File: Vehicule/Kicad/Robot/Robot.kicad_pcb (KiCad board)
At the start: 2 copper layers, 60 x 50 mm, 3 parts, among them U1 ESP32-C3_SUPERMINI, U2 L293D, U3 Regulator-DFR0569

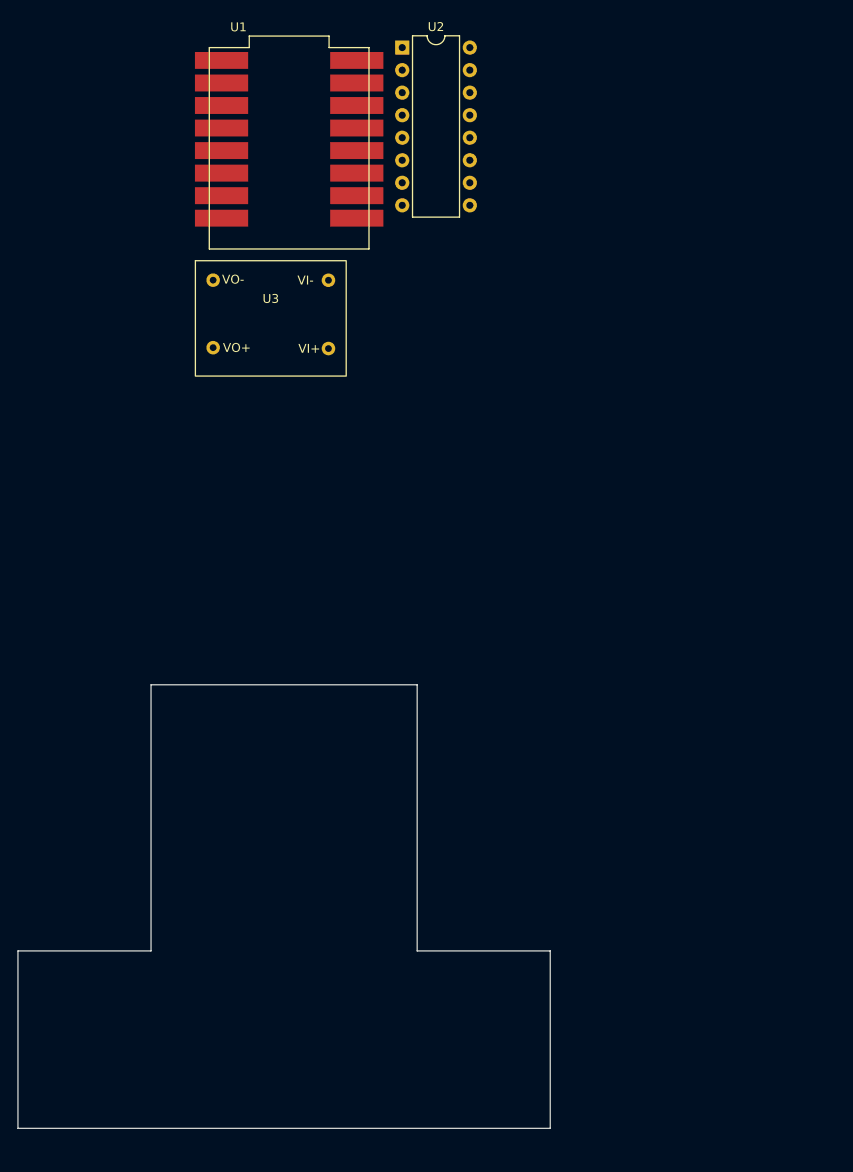
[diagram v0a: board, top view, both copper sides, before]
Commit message: Schema et implantation du circuit pour le robot
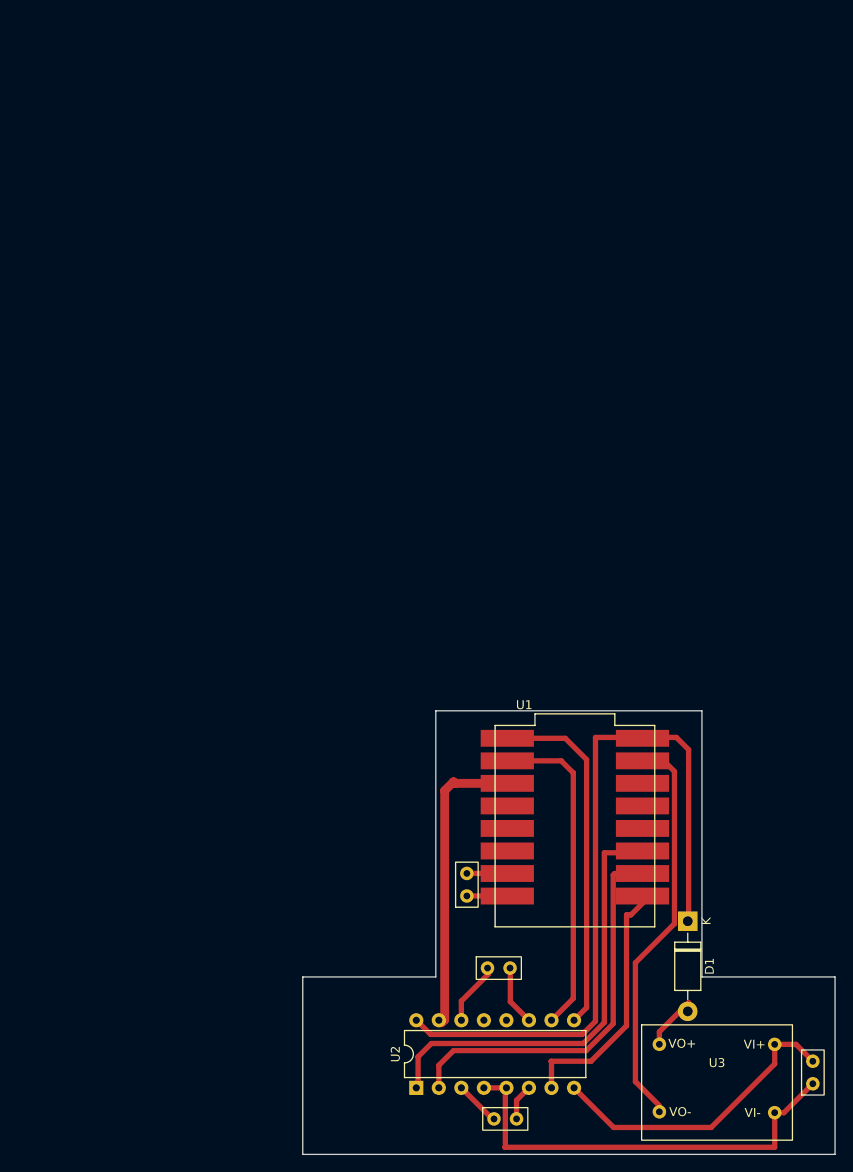
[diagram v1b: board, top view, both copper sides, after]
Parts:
- added D1: 1N5818, Diode_THT:D_DO-41_SOD81_P10.16mm_Horizontal, F.Cu at (115.5, 126.7)
- added J1: Conn_01x02_Socket, Empreintes:CONN-2-PINS, F.Cu at (129.6, 143.7)
- added J2: Conn_01x02_Socket, Empreintes:CONN-2-PINS, F.Cu at (90.6, 122.5)
- added J3: Conn_01x02_Socket, Empreintes:CONN-2-PINS, F.Cu at (94.2, 131.9)
- added J4: Conn_01x02_Socket, Empreintes:CONN-2-PINS, F.Cu at (94.9, 148.9)
- U3: value Regulator-DFR0569 -> ~
- moved U2 117.3 mm to (84.9, 145.4), turned to 90 degrees
- moved U3 99.7 mm to (118.8, 144.3)
- moved U1 82.9 mm to (102.8, 115.9)
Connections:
- U1 pad 0: unconnected-(U1-GPIO0-Pad0) -> Net-(U1-GPIO0)
- U1 pad 1: unconnected-(U1-GPIO1-Pad1) -> Net-(U1-GPIO1)
- U1 pad 2: unconnected-(U1-GPIO2-Pad2) -> Net-(U1-GPIO2)
- U1 pad 20: unconnected-(U1-GPIO20-Pad20) -> Net-(J2-Pin_2)
- U1 pad 21: unconnected-(U1-GPIO21-Pad21) -> Net-(J2-Pin_1)
- U1 pad 3.3: unconnected-(U1-3V3-Pad3.3) -> Net-(U1-3V3)
- U1 pad 5: unconnected-(U1-GPIO5-Pad5) -> Net-(U1-GPIO5)
- U1 pad 5V: unconnected-(U1-Pad5V) -> Net-(D1-K)
- U1 pad 6: unconnected-(U1-GPIO6-Pad6) -> Net-(U1-GPIO6)
- U1 pad 7: unconnected-(U1-GPIO7-Pad7) -> Net-(U1-GPIO7)
- U1 pad G: unconnected-(U1-GND-PadG) -> GND
- U2 pad 1: unconnected-(U2-EN1,2-Pad1) -> Net-(U1-GPIO2)
- U2 pad 10: unconnected-(U2-3A-Pad10) -> Net-(U1-GPIO6)
- U2 pad 11: unconnected-(U2-3Y-Pad11) -> Net-(J3-Pin_2)
- U2 pad 14: unconnected-(U2-4Y-Pad14) -> Net-(J3-Pin_1)
- U2 pad 15: unconnected-(U2-4A-Pad15) -> Net-(U1-GPIO7)
- U2 pad 16: unconnected-(U2-VCC1-Pad16) -> Net-(D1-K)
- U2 pad 2: unconnected-(U2-1A-Pad2) -> Net-(U1-GPIO1)
- U2 pad 3: unconnected-(U2-1Y-Pad3) -> Net-(J4-Pin_1)
- U2 pad 4: unconnected-(U2-GND-Pad4) -> GND
- U2 pad 5: unconnected-(U2-GND-Pad5) -> GND
- U2 pad 6: unconnected-(U2-2Y-Pad6) -> Net-(J4-Pin_2)
- U2 pad 7: unconnected-(U2-2A-Pad7) -> Net-(U1-GPIO0)
- U2 pad 8: unconnected-(U2-VCC2-Pad8) -> Net-(J1-Pin_2)
- U2 pad 9: unconnected-(U2-EN3,4-Pad9) -> Net-(U1-GPIO5)
- U3 pad 1: unconnected-(U3-VO--Pad1) -> Net-(D1-A)
- U3 pad 2: unconnected-(U3-VO+-Pad2) -> GND
- U3 pad 3: unconnected-(U3-VI--Pad3) -> Net-(J1-Pin_2)
- U3 pad 4: unconnected-(U3-VI+-Pad4) -> GND
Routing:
- net GND: track 0.00 -> 94.0 mm
- net Net-(D1-K): track 0.00 -> 81.6 mm
- net Net-(U1-GPIO2): track 0.00 -> 49.7 mm
- net Net-(U1-GPIO1): track 0.00 -> 45.1 mm
- net Net-(U1-GPIO5): track 0.00 -> 39.1 mm
- net Net-(U1-GPIO6): track 0.00 -> 36.1 mm
- net Net-(J1-Pin_2): track 0.00 -> 34.7 mm
- net Net-(U1-GPIO7): track 0.00 -> 33.2 mm
- net Net-(U1-GPIO0): track 0.00 -> 29.2 mm
- net Net-(J3-Pin_1): track 0.00 -> 6.55 mm
- net Net-(J3-Pin_2): track 0.00 -> 6.15 mm
- net Net-(J2-Pin_2): track 0.00 -> 5.38 mm
- net Net-(J2-Pin_1): track 0.00 -> 5.38 mm
- net Net-(D1-A): track 0.00 -> 5.38 mm
- net Net-(J4-Pin_1): track 0.00 -> 5.13 mm
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
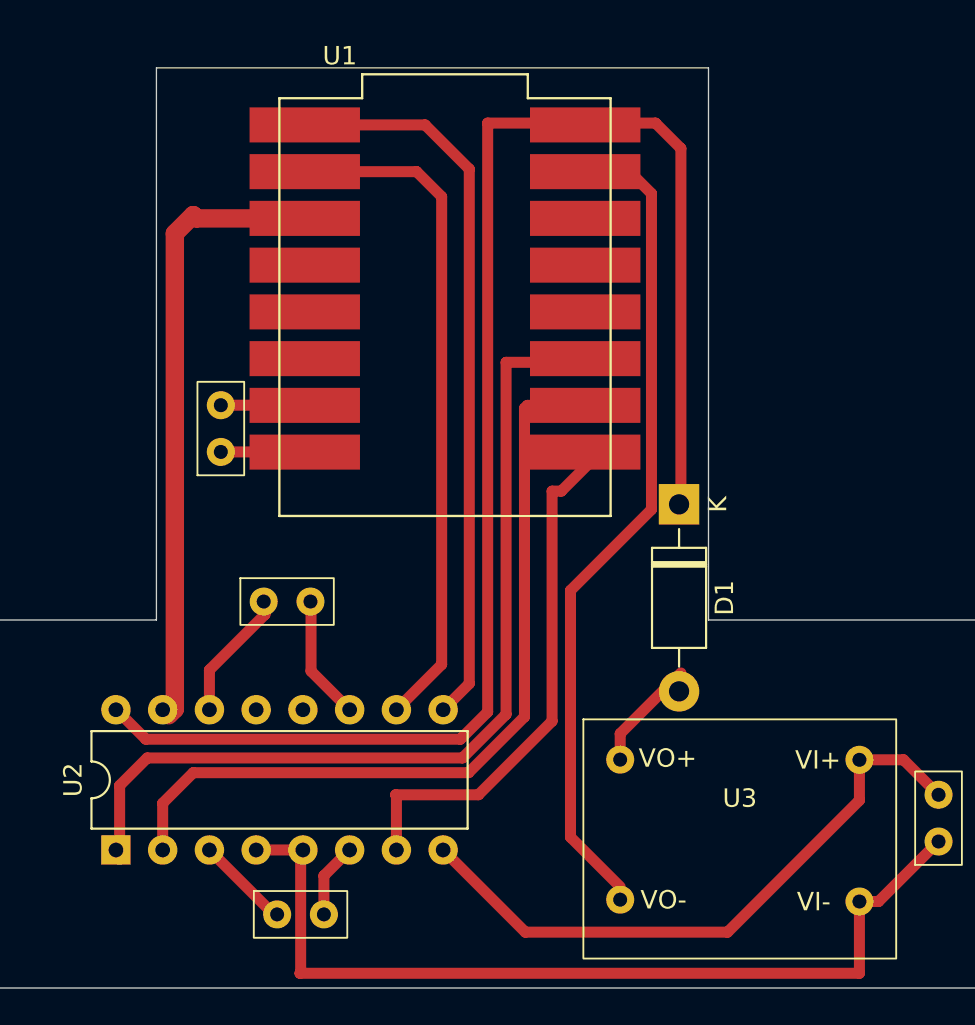
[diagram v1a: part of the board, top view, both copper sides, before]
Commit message: Transfert du SUPERMINI (composant et empreintes) dans les librairies locales (Anumby et Empreintes) Renommer Empreintes -> Anumby
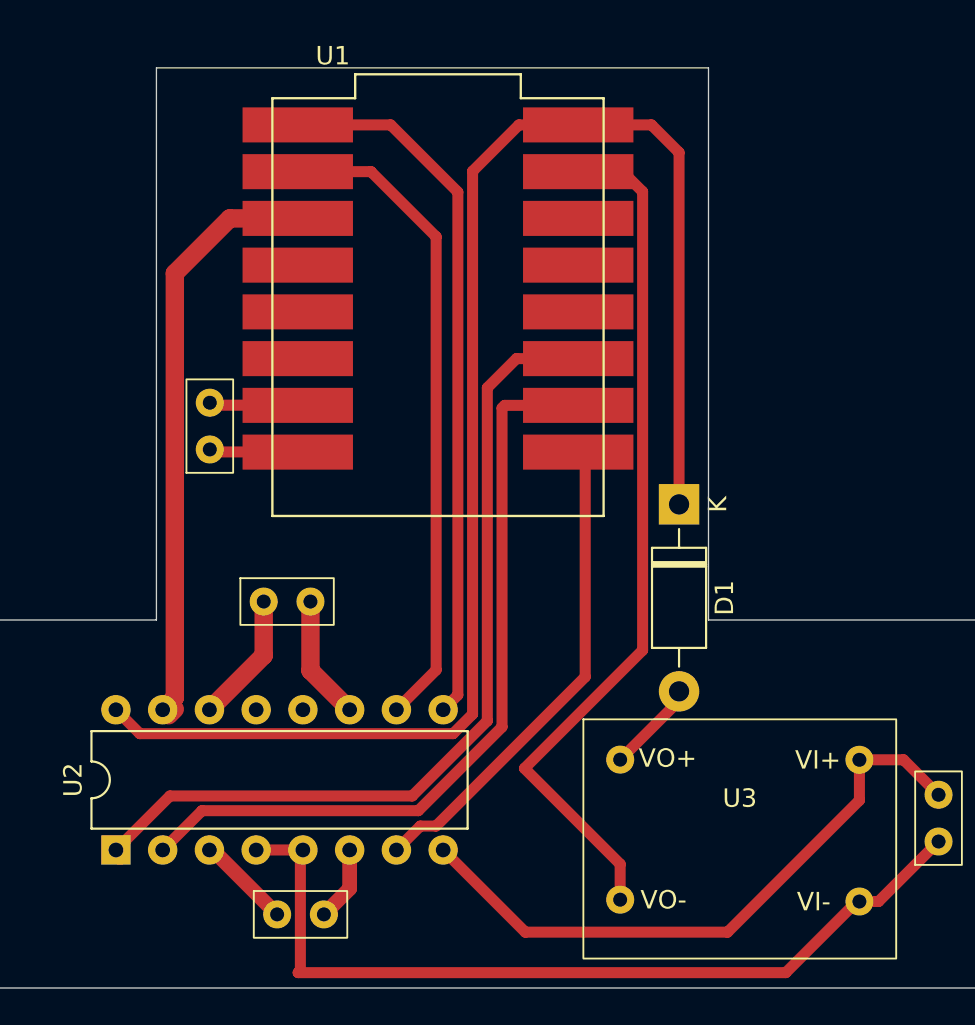
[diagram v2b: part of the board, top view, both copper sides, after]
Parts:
- J1, J2, J3, J4: footprint Empreintes:CONN-2-PINS -> Anumby:CONN-2-PINS
- U1: footprint PCM_Espressif:ESP32-C3-SUPERMINI -> Anumby:ESP32-C3-SUPERMINI
- U3: footprint Empreintes:Regulator-DFR0569 -> Anumby:Regulator-DFR0569
- moved J2 0.61 mm to (90.0, 122.4)
- moved U1 0.38 mm to (102.4, 115.9)
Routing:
- net Net-(U1-GPIO0): track 29.2 -> 26.4 mm
- net Net-(U1-GPIO2): track 49.7 -> 47.7 mm
- net Net-(U1-GPIO6): track 36.1 -> 35.2 mm
- net Net-(J2-Pin_1): track 5.38 -> 4.58 mm
- net Net-(J2-Pin_2): track 5.38 -> 4.58 mm
- net Net-(U1-GPIO5): track 39.1 -> 38.3 mm
- net Net-(J3-Pin_2): track 6.15 -> 6.76 mm
- net GND: track 94.0 -> 94.6 mm
- net Net-(J3-Pin_1): track 6.55 -> 7.10 mm

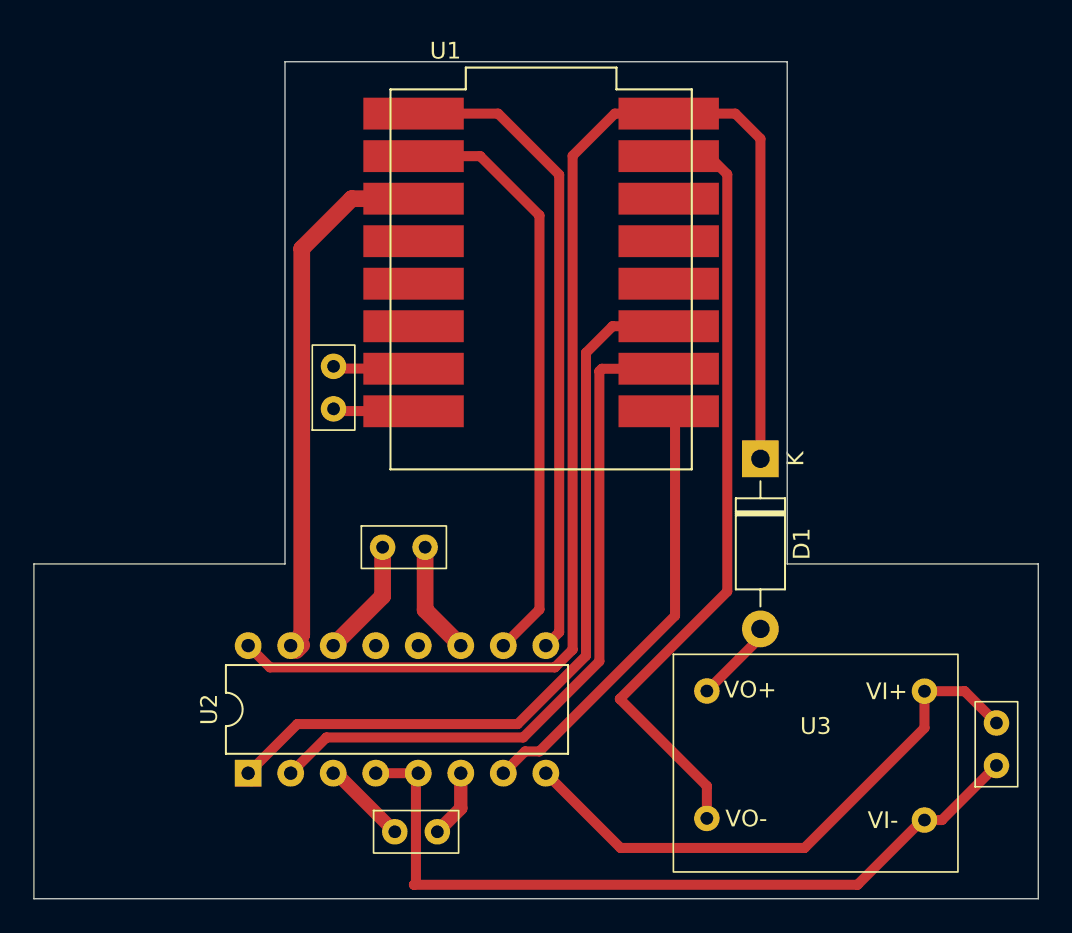
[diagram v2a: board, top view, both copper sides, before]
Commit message: Ajout de la couche de masse pour Robot Ajout d'un connecteur 1 pin Mise à jour de tous les PCB et les Schémas
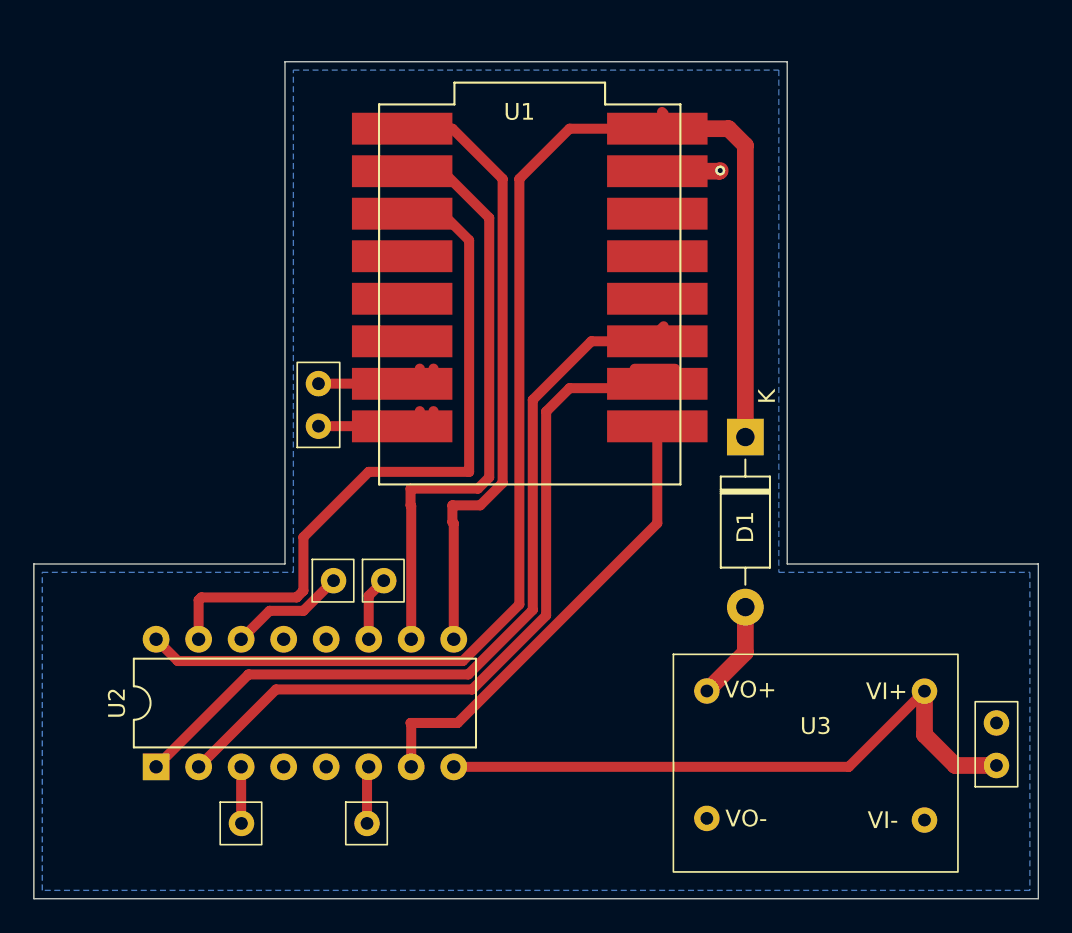
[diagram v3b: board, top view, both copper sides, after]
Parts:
- added J5: Conn_01x01_Socket, Anumby:CONN-1-PINS, F.Cu at (93.3, 148.4)
- added J6: Conn_01x01_Socket, Anumby:CONN-1-PINS, F.Cu at (85.8, 148.4)
- J3, J4: value Conn_01x02_Socket -> Conn_01x01_Socket; footprint Anumby:CONN-2-PINS -> Anumby:CONN-1-PINS
- moved J4 15.0 mm to (94.3, 133.9)
- moved U2 5.51 mm to (79.4, 145.1)
- moved J3 3.55 mm to (91.3, 133.9)
- moved D1 1.58 mm to (114.6, 125.4)
- moved J2 1.37 mm to (89.1, 123.4)
- moved U1 1.13 mm to (101.7, 116.8)
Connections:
- J1 pad 1: GND -> Net-(J1-Pin_1)
- J1 pad 2: Net-(J1-Pin_2) -> GND
- U2 pad 11: Net-(J3-Pin_2) -> Net-(J4-Pin_1)
- U2 pad 3: Net-(J4-Pin_1) -> Net-(J6-Pin_1)
- U2 pad 6: Net-(J4-Pin_2) -> Net-(J5-Pin_1)
- U2 pad 8: Net-(J1-Pin_2) -> Net-(J1-Pin_1)
- U3 pad 3: Net-(J1-Pin_2) -> Net-(J1-Pin_1)
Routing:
- net GND: track 94.6 -> 4.18 mm, vias 0 -> 1
- net Net-(J1-Pin_1): track 0.00 -> 37.7 mm
- net Net-(J1-Pin_2): track 34.7 -> 0.00 mm
- net Net-(U1-GPIO7): track 32.8 -> 42.0 mm
- net Net-(J3-Pin_2): track 6.76 -> 0.00 mm
- net Net-(J4-Pin_2): track 4.08 -> 0.00 mm
- net Net-(J5-Pin_1): track 0.00 -> 3.82 mm
- net Net-(J6-Pin_1): track 0.00 -> 3.39 mm
- net Net-(U1-GPIO0): track 26.4 -> 28.1 mm
- net Net-(J4-Pin_1): track 5.31 -> 3.93 mm
- net Net-(U1-GPIO5): track 38.3 -> 37.0 mm
- net Net-(U1-GPIO1): track 45.2 -> 46.4 mm
- net Net-(D1-A): track 5.04 -> 5.96 mm
- net Net-(U1-GPIO6): track 35.2 -> 35.9 mm
- added copper zone on B.Cu, net GND

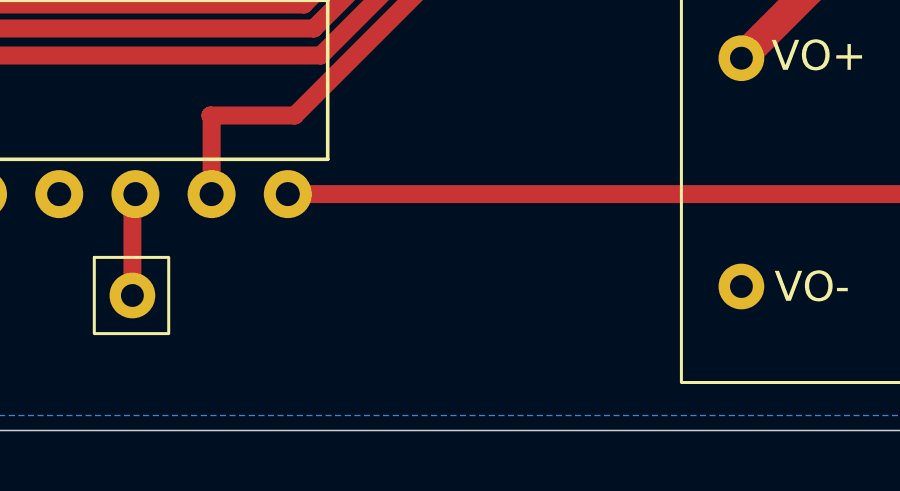
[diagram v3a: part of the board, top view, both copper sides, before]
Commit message: Ajout de logo Anumby pour PCB (2 versions)
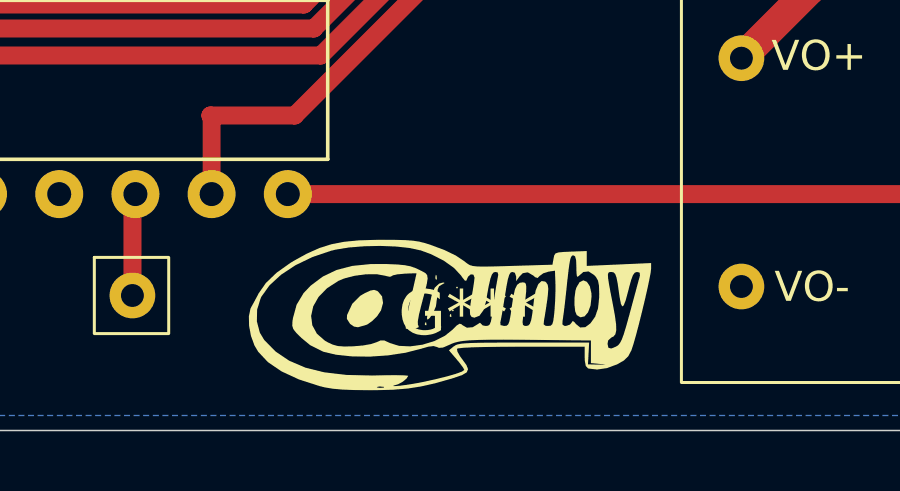
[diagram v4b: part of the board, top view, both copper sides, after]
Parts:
- added G***: LOGO, Anumby:Logo_Anumby_15, F.Cu at (103.2, 149.0)

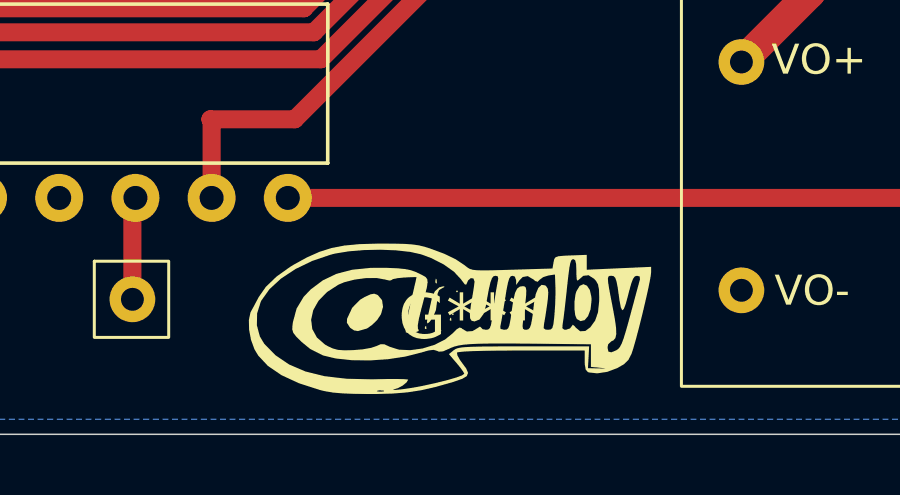
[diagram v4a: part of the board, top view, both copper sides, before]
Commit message: Ajout de logo Anumby pour PCB
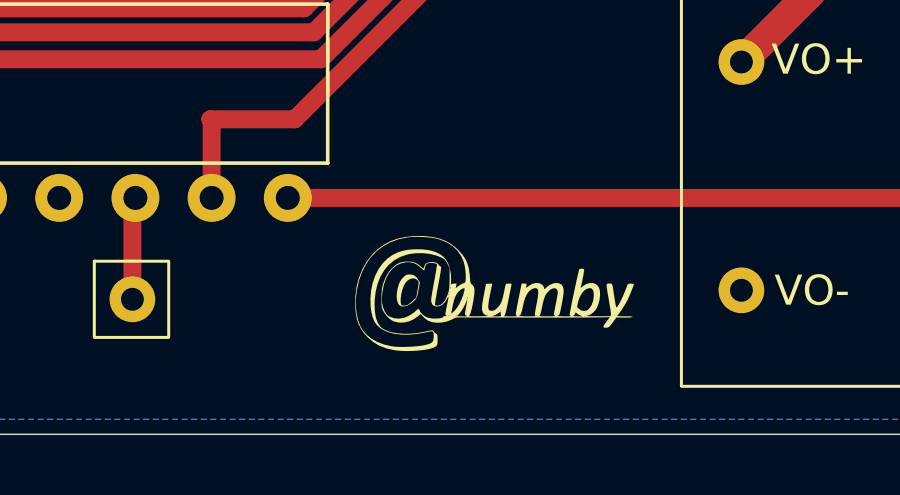
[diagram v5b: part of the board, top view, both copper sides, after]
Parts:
- removed G***: LOGO, Anumby:Logo_Anumby_15
- added G: Val**, Anumby:Logo_Anumby_10, F.Cu at (104.1, 148.2)
